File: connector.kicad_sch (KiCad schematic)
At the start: 174 parts, among them J1 USB_C_Receptacle_USB2.0_16P, J10 POWER2, J11 TELEM1, J12 TELEM2, J13 GPS, J14 SERIAL4, J15 SERIAL5, J16 I2C, J17 CAN, J18 BUZZER, J19 Conn_01x05_Pin, J2 Micro_SD_Card_Det1, J20 ADC, J21 SPI, J22 SAFETY, J23 CAN2, J24 SBUS, J25 Channel 1, J26 Channel 2, J27 Channel 3, J28 Channel 4, J41 Channel 5, J42 Channel 6, J43 Channel 7, J44 Channel 8, J45 Channel 13, J46 Channel 9, J47 Channel 14, J48 Channel 10, J49 Channel 15, J50 Channel 11, J51 Channel 16, J52 Channel 12, J9 POWER1, Q1 AO3400A, U12 USBLC6-2SC6, U16 TPS2553DBVT, U17 TPS2553DBVT, U18 TPS2553DBVT, U19 TPS2553DBVT, U20 TPS2553DBVT, U21 TPS2553DBVT, U22 TPS2553DBVT, U23 TPS2553DBVT, U24 TPS2553DBVT

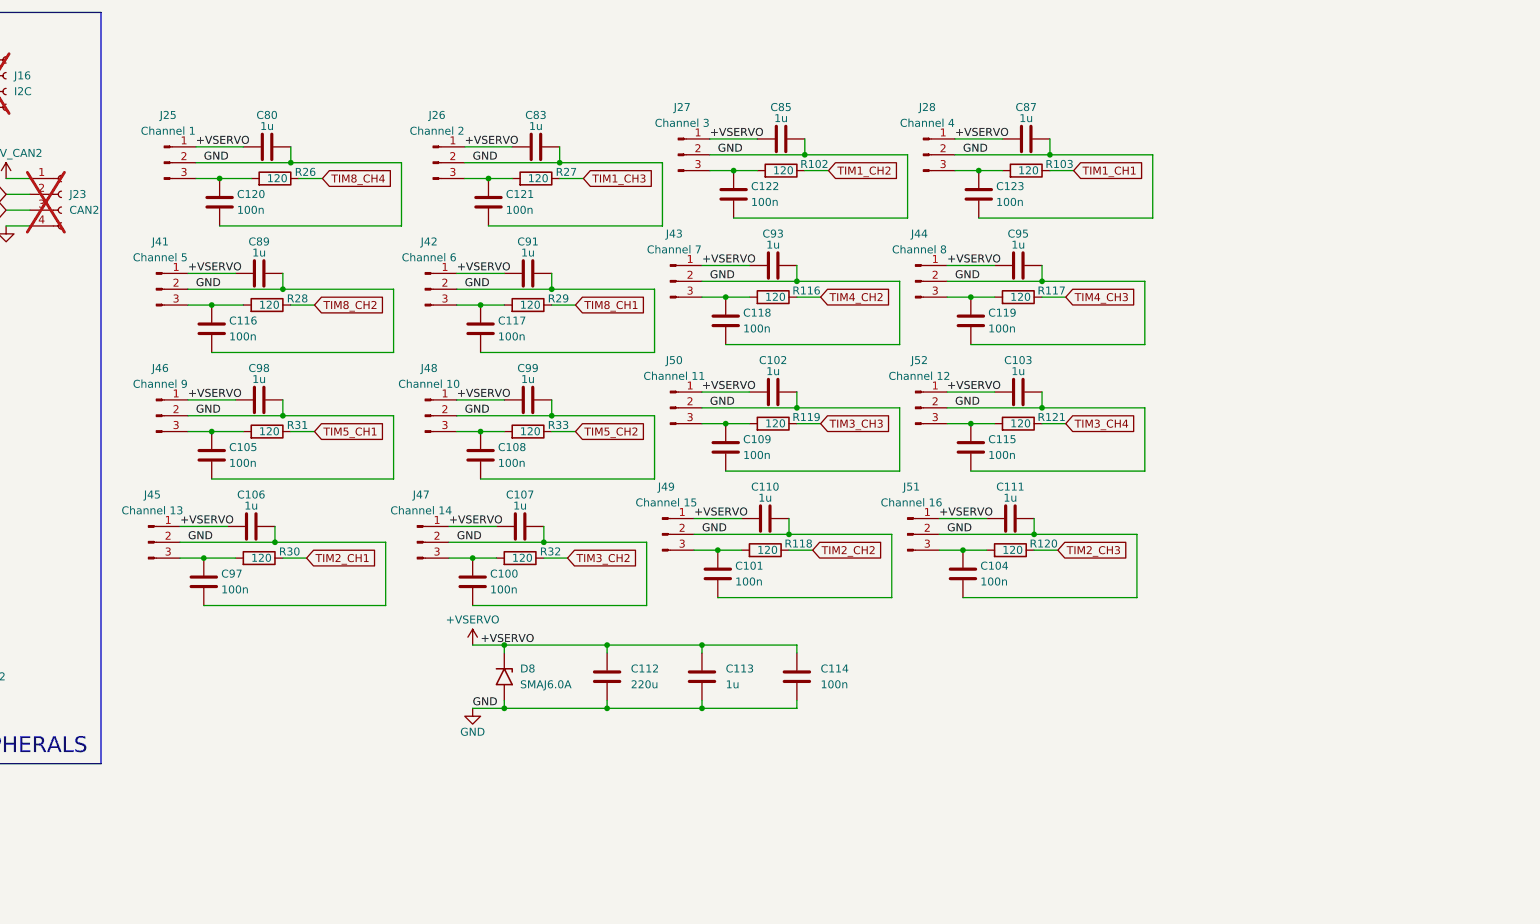
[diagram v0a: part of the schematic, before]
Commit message: Connector: re-annotate kanal (J30-40/J53-57) + reorder pin [S,V+,GND] (verified, ERC 0E/17W)
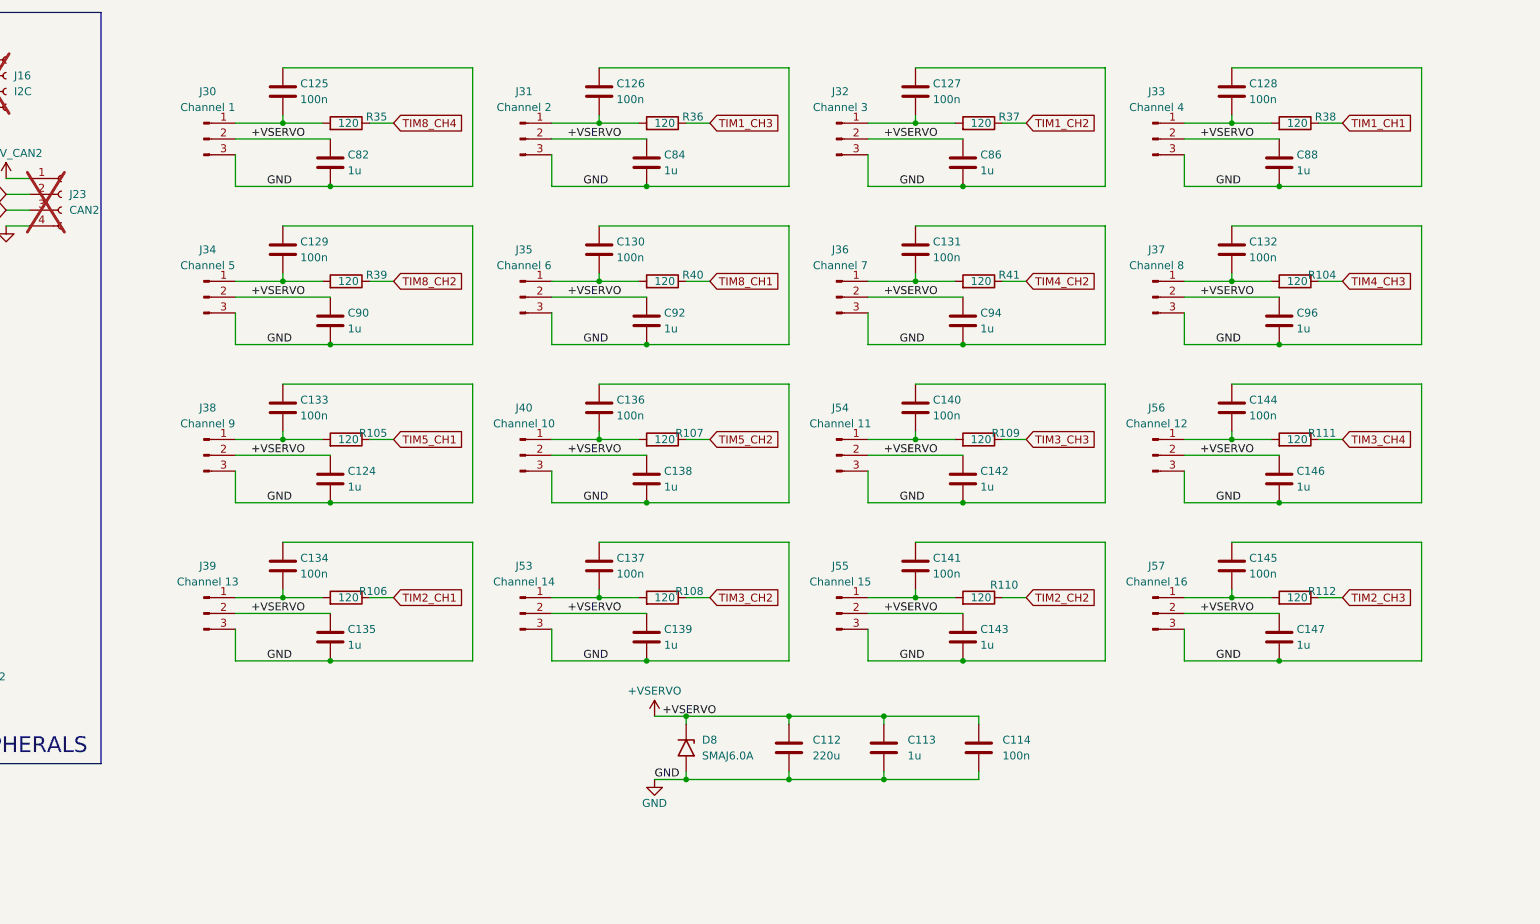
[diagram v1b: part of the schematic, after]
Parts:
- removed C100, C101, C104, C105, C108, C109, C115, C116, C117, C118, C119, C120, C121, C122, C123, C97: 100n, Capacitor_SMD:C_0402_1005Metric, symbol Device:C
- removed C102, C103, C106, C107, C110, C111, C80, C83, C85, C87, C89, C91, C93, C95, C98, C99: 1u, Capacitor_SMD:C_0603_1608Metric, symbol Device:C
- removed J25: Channel 1, symbol Connector:Conn_01x03_Pin
- removed J26: Channel 2, symbol Connector:Conn_01x03_Pin
- removed J27: Channel 3, symbol Connector:Conn_01x03_Pin
- removed J28: Channel 4, symbol Connector:Conn_01x03_Pin
- removed J41: Channel 5, symbol Connector:Conn_01x03_Pin
- removed J42: Channel 6, symbol Connector:Conn_01x03_Pin
- removed J43: Channel 7, symbol Connector:Conn_01x03_Pin
- removed J44: Channel 8, symbol Connector:Conn_01x03_Pin
- removed J45: Channel 13, symbol Connector:Conn_01x03_Pin
- removed J46: Channel 9, symbol Connector:Conn_01x03_Pin
- removed J47: Channel 14, symbol Connector:Conn_01x03_Pin
- removed J48: Channel 10, symbol Connector:Conn_01x03_Pin
- removed J49: Channel 15, symbol Connector:Conn_01x03_Pin
- removed J50: Channel 11, symbol Connector:Conn_01x03_Pin
- removed J51: Channel 16, symbol Connector:Conn_01x03_Pin
- removed J52: Channel 12, symbol Connector:Conn_01x03_Pin
- removed R102, R103, R116, R117, R118, R119, R120, R121, R26, R27, R28, R29, R30, R31, R32, R33: 120, Resistor_SMD:R_0402_1005Metric, symbol Device:R
- added C124, C135, C138, C139, C142, C143, C146, C147, C82, C84, C86, C88, C90, C92, C94, C96: 1u, symbol Device:C
- added C125, C126, C127, C128, C129, C130, C131, C132, C133, C134, C136, C137, C140, C141, C144, C145: 100n, Capacitor_SMD:C_0402_1005Metric, symbol Device:C
- added J30: Channel 1, Connector_JST:JST_XH_B3B-XH-A_1x03_P2.50mm_Vertical, symbol Connector:Conn_01x03_Pin
- added J31: Channel 2, Connector_JST:JST_XH_B3B-XH-A_1x03_P2.50mm_Vertical, symbol Connector:Conn_01x03_Pin
- added J32: Channel 3, Connector_JST:JST_XH_B3B-XH-A_1x03_P2.50mm_Vertical, symbol Connector:Conn_01x03_Pin
- added J33: Channel 4, Connector_JST:JST_XH_B3B-XH-A_1x03_P2.50mm_Vertical, symbol Connector:Conn_01x03_Pin
- added J34: Channel 5, Connector_JST:JST_XH_B3B-XH-A_1x03_P2.50mm_Vertical, symbol Connector:Conn_01x03_Pin
- added J35: Channel 6, Connector_JST:JST_XH_B3B-XH-A_1x03_P2.50mm_Vertical, symbol Connector:Conn_01x03_Pin
- added J36: Channel 7, Connector_JST:JST_XH_B3B-XH-A_1x03_P2.50mm_Vertical, symbol Connector:Conn_01x03_Pin
- added J37: Channel 8, Connector_JST:JST_XH_B3B-XH-A_1x03_P2.50mm_Vertical, symbol Connector:Conn_01x03_Pin
- added J38: Channel 9, Connector_JST:JST_XH_B3B-XH-A_1x03_P2.50mm_Vertical, symbol Connector:Conn_01x03_Pin
- added J39: Channel 13, Connector_JST:JST_XH_B3B-XH-A_1x03_P2.50mm_Vertical, symbol Connector:Conn_01x03_Pin
- added J40: Channel 10, Connector_JST:JST_XH_B3B-XH-A_1x03_P2.50mm_Vertical, symbol Connector:Conn_01x03_Pin
- added J53: Channel 14, Connector_JST:JST_XH_B3B-XH-A_1x03_P2.50mm_Vertical, symbol Connector:Conn_01x03_Pin
- added J54: Channel 11, Connector_JST:JST_XH_B3B-XH-A_1x03_P2.50mm_Vertical, symbol Connector:Conn_01x03_Pin
- added J55: Channel 15, Connector_JST:JST_XH_B3B-XH-A_1x03_P2.50mm_Vertical, symbol Connector:Conn_01x03_Pin
- added J56: Channel 12, Connector_JST:JST_XH_B3B-XH-A_1x03_P2.50mm_Vertical, symbol Connector:Conn_01x03_Pin
- added J57: Channel 16, Connector_JST:JST_XH_B3B-XH-A_1x03_P2.50mm_Vertical, symbol Connector:Conn_01x03_Pin
- added R104, R105, R106, R107, R108, R109, R110, R111, R112, R35, R36, R37, R38, R39, R40, R41: 120, Resistor_SMD:R_0402_1005Metric, symbol Device:R
- J24: footprint Connector_PinHeader_2.54mm:PinHeader_1x03_P2.54mm_Vertical -> Connector_JST:JST_GH_BM03B-GHS-TBT_1x03-1MP_P1.25mm_Vertical
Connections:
- net +VSERVO: now also C124.1, C135.1, C138.1, C139.1, C142.1, C143.1, C146.1, C147.1, C82.1, C84.1, C86.1, C88.1, C90.1, C92.1, C94.1, C96.1, J30.2 (Pin_2), J31.2 (Pin_2), J32.2 (Pin_2), J33.2 (Pin_2), J34.2 (Pin_2), J35.2 (Pin_2), J36.2 (Pin_2), J37.2 (Pin_2), J38.2 (Pin_2), J39.2 (Pin_2), J40.2 (Pin_2), J53.2 (Pin_2), J54.2 (Pin_2), J55.2 (Pin_2), J56.2 (Pin_2), J57.2 (Pin_2)
- net GND: now also C124.2, C125.1, C126.1, C127.1, C128.1, C129.1, C130.1, C131.1, C132.1, C133.1, C134.1, C135.2, C136.1, C137.1, C138.2, C139.2, C140.1, C141.1, C142.2, C143.2, C144.1, C145.1, C146.2, C147.2, C82.2, C84.2, C86.2, C88.2, C90.2, C92.2, C94.2, C96.2, J30.3 (Pin_3), J31.3 (Pin_3), J32.3 (Pin_3), J33.3 (Pin_3), J34.3 (Pin_3), J35.3 (Pin_3), J36.3 (Pin_3), J37.3 (Pin_3), J38.3 (Pin_3), J39.3 (Pin_3), J40.3 (Pin_3), J53.3 (Pin_3), J54.3 (Pin_3), J55.3 (Pin_3), J56.3 (Pin_3), J57.3 (Pin_3)
- net TIM1_CH1: now also R38.1
- net TIM1_CH2: now also R37.1
- net TIM1_CH3: now also R36.1
- net TIM2_CH1: now also R106.1
- net TIM2_CH2: now also R110.1
- net TIM2_CH3: now also R112.1
- net TIM3_CH2: now also R108.1
- net TIM3_CH3: now also R109.1
- net TIM3_CH4: now also R111.1
- net TIM4_CH2: now also R41.1
- net TIM4_CH3: now also R104.1
- net TIM5_CH1: now also R105.1
- net TIM5_CH2: now also R107.1
- net TIM8_CH1: now also R40.1
- net TIM8_CH2: now also R39.1
- net TIM8_CH4: now also R35.1
- new net: C133.2, J38.1 (Pin_1), R105.2
- new net: C140.2, J54.1 (Pin_1), R109.2
- new net: C145.2, J57.1 (Pin_1), R112.2
- new net: C136.2, J40.1 (Pin_1), R107.2
- new net: C134.2, J39.1 (Pin_1), R106.2
- new net: C137.2, J53.1 (Pin_1), R108.2
- new net: C129.2, J34.1 (Pin_1), R39.2
- new net: C126.2, J31.1 (Pin_1), R36.2
- new net: C144.2, J56.1 (Pin_1), R111.2
- new net: C130.2, J35.1 (Pin_1), R40.2
- new net: C132.2, J37.1 (Pin_1), R104.2
- new net: C131.2, J36.1 (Pin_1), R41.2
- new net: C128.2, J33.1 (Pin_1), R38.2
- new net: C125.2, J30.1 (Pin_1), R35.2
- new net: C127.2, J32.1 (Pin_1), R37.2
- new net: C141.2, J55.1 (Pin_1), R110.2
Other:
- moved on the sheet: C112, C113, C114, D8
